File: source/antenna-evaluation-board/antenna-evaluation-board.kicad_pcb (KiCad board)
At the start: 4 copper layers, 129 x 69 mm, 41 parts, among them J1 Conn_Coaxial, J10 Conn_Coaxial, J2 Conn_Coaxial, J3 Conn_Coaxial, J4 Conn_Coaxial, J5 Conn_Coaxial, J6 Conn_Coaxial, J7 Conn_Coaxial, J8 Conn_Coaxial, J9 Conn_Coaxial

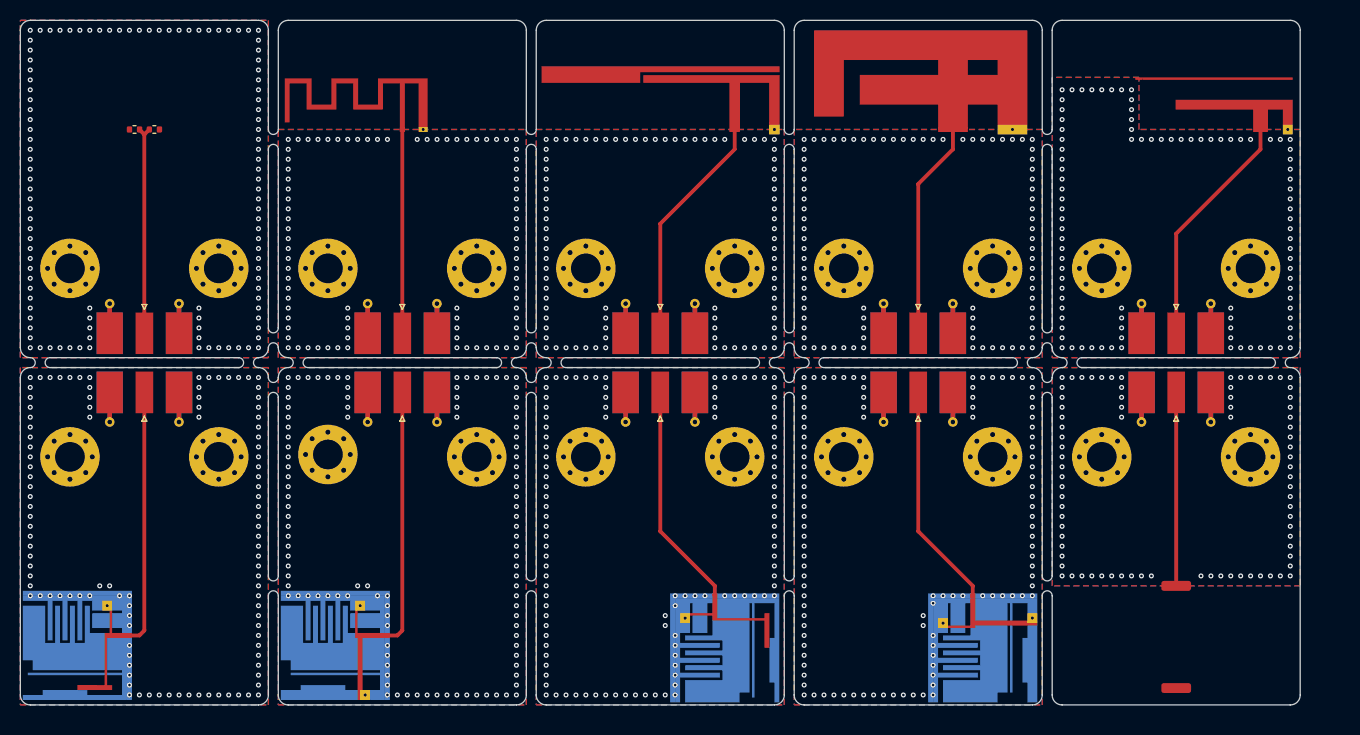
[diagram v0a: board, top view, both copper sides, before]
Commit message: use tons of drils instead of v cuts
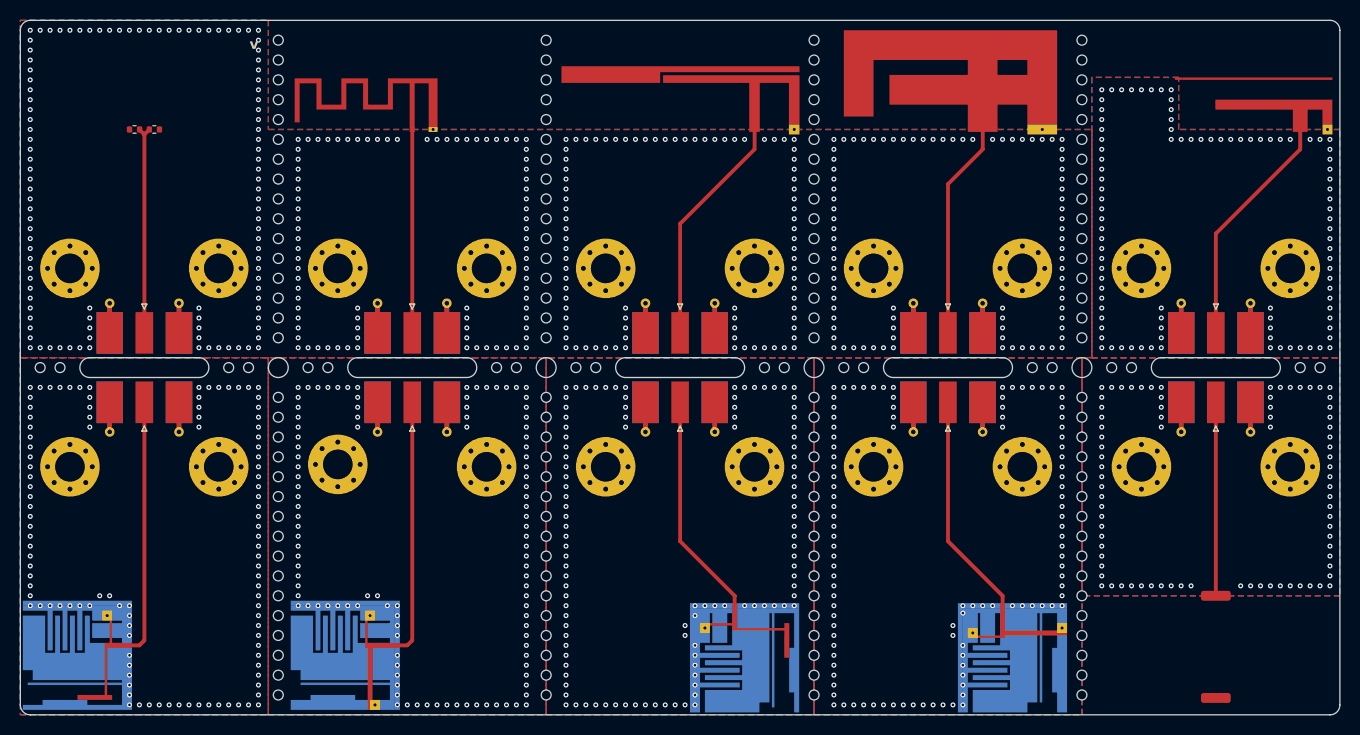
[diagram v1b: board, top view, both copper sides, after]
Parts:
- added REF**: MountingHole_2.1mm, MountingHole:MountingHole_2.1mm, F.Cu at (137.0, 81.0)
- added REF**: MountingHole_2.1mm, MountingHole:MountingHole_2.1mm, F.Cu at (137.0, 63.0)
- added REF**: MountingHole_2.1mm, MountingHole:MountingHole_2.1mm, F.Cu at (78.0, 74.0)
- added REF**: MountingHole_2.1mm, MountingHole:MountingHole_2.1mm, F.Cu at (110.0, 53.0)
- added REF**: MountingHole_2.1mm, MountingHole:MountingHole_2.1mm, F.Cu at (110.0, 93.0)
- added REF**: MountingHole_2.1mm, MountingHole:MountingHole_2.1mm, F.Cu at (137.0, 79.0)
- added REF**: MountingHole_2.1mm, MountingHole:MountingHole_2.1mm, F.Cu at (32.0, 74.0)
- added REF**: MountingHole_2.1mm, MountingHole:MountingHole_2.1mm, F.Cu at (56.0, 89.0)
- added REF**: MountingHole_2.1mm, MountingHole:MountingHole_2.1mm, F.Cu at (83.0, 87.0)
- added REF**: MountingHole_2.1mm, MountingHole:MountingHole_2.1mm, F.Cu at (110.0, 67.0)
- added REF**: MountingHole_2.1mm, MountingHole:MountingHole_2.1mm, F.Cu at (110.0, 47.0)
- added REF**: MountingHole_2.1mm, MountingHole:MountingHole_2.1mm, F.Cu at (137.0, 93.0)
- added REF**: MountingHole_2.1mm, MountingHole:MountingHole_2.1mm, F.Cu at (56.0, 65.0)
- added REF**: MountingHole_2.1mm, MountingHole:MountingHole_2.1mm, F.Cu at (83.0, 43.0)
- added REF**: MountingHole_2.1mm, MountingHole:MountingHole_2.1mm, F.Cu at (83.0, 97.0)
- added REF**: MountingHole_2.1mm, MountingHole:MountingHole_2.1mm, F.Cu at (83.0, 81.0)
- added REF**: MountingHole_2.1mm, MountingHole:MountingHole_2.1mm, F.Cu at (137.0, 43.0)
- added REF**: MountingHole_2.1mm, MountingHole:MountingHole_2.1mm, F.Cu at (83.0, 55.0)
- added REF**: MountingHole_2.1mm, MountingHole:MountingHole_2.1mm, F.Cu at (83.0, 41.0)
- added REF**: MountingHole_2.1mm, MountingHole:MountingHole_2.1mm, F.Cu at (110.0, 89.0)
- added REF**: MountingHole_2.1mm, MountingHole:MountingHole_2.1mm, F.Cu at (110.0, 61.0)
- added REF**: MountingHole_2.1mm, MountingHole:MountingHole_2.1mm, F.Cu at (56.0, 97.0)
- added REF**: MountingHole_2.1mm, MountingHole:MountingHole_2.1mm, F.Cu at (140.0, 74.0)
- added REF**: MountingHole_2.1mm, MountingHole:MountingHole_2.1mm, F.Cu at (137.0, 101.0)
- added REF**: MountingHole_2.1mm, MountingHole:MountingHole_2.1mm, F.Cu at (110.0, 83.0)
- added REF**: MountingHole_2.1mm, MountingHole:MountingHole_2.1mm, F.Cu at (115.0, 74.0)
- added REF**: MountingHole_2.1mm, MountingHole:MountingHole_2.1mm, F.Cu at (56.0, 101.0)
- added REF**: MountingHole_2.1mm, MountingHole:MountingHole_2.1mm, F.Cu at (110.0, 95.0)
- added REF**: MountingHole_2.1mm, MountingHole:MountingHole_2.1mm, F.Cu at (83.0, 53.0)
- added REF**: MountingHole_2.1mm, MountingHole:MountingHole_2.1mm, F.Cu at (110.0, 59.0)
- added REF**: MountingHole_2.1mm, MountingHole:MountingHole_2.1mm, F.Cu at (137.0, 71.0)
- added REF**: MountingHole_2.1mm, MountingHole:MountingHole_2.1mm, F.Cu at (83.0, 65.0)
- added REF**: MountingHole_2.1mm, MountingHole:MountingHole_2.1mm, F.Cu at (83.0, 47.0)
- added REF**: MountingHole_2.1mm, MountingHole:MountingHole_2.1mm, F.Cu at (113.0, 74.0)
- added REF**: MountingHole_2.1mm, MountingHole:MountingHole_2.1mm, F.Cu at (110.0, 97.0)
- added REF**: MountingHole_2.1mm, MountingHole:MountingHole_2.1mm, F.Cu at (110.0, 85.0)
- added REF**: MountingHole_2.1mm, MountingHole:MountingHole_2.1mm, F.Cu at (56.0, 81.0)
- added REF**: MountingHole_2.1mm, MountingHole:MountingHole_2.1mm, F.Cu at (83.0, 71.0)
- added REF**: MountingHole_2.1mm, MountingHole:MountingHole_2.1mm, F.Cu at (110.0, 57.0)
- added REF**: MountingHole_2.1mm, MountingHole:MountingHole_2.1mm, F.Cu at (83.0, 105.0)
- added REF**: MountingHole_2.1mm, MountingHole:MountingHole_2.1mm, F.Cu at (83.0, 67.0)
- added REF**: MountingHole_2.1mm, MountingHole:MountingHole_2.1mm, F.Cu at (56.0, 83.0)
- added REF**: MountingHole_2.1mm, MountingHole:MountingHole_2.1mm, F.Cu at (110.0, 63.0)
- added REF**: MountingHole_2.1mm, MountingHole:MountingHole_2.1mm, F.Cu at (56.0, 103.0)
- added REF**: MountingHole_2.1mm, MountingHole:MountingHole_2.1mm, F.Cu at (56.0, 95.0)
- added REF**: MountingHole_2.1mm, MountingHole:MountingHole_2.1mm, F.Cu at (34.0, 74.0)
- added REF**: MountingHole_2.1mm, MountingHole:MountingHole_2.1mm, F.Cu at (110.0, 99.0)
- added REF**: MountingHole_2.1mm, MountingHole:MountingHole_2.1mm, F.Cu at (137.0, 83.0)
- added REF**: MountingHole_2.1mm, MountingHole:MountingHole_2.1mm, F.Cu at (83.0, 61.0)
- added REF**: MountingHole_2.1mm, MountingHole:MountingHole_2.1mm, F.Cu at (137.0, 49.0)
- added REF**: MountingHole_2.1mm, MountingHole:MountingHole_2.1mm, F.Cu at (56.0, 87.0)
- added REF**: MountingHole_2.1mm, MountingHole:MountingHole_2.1mm, F.Cu at (134.0, 74.0)
- added REF**: MountingHole_2.1mm, MountingHole:MountingHole_2.1mm, F.Cu at (161.0, 74.0)
- added REF**: MountingHole_2.1mm, MountingHole:MountingHole_2.1mm, F.Cu at (137.0, 41.0)
- added REF**: MountingHole_2.1mm, MountingHole:MountingHole_2.1mm, F.Cu at (56.0, 93.0)
- added REF**: MountingHole_2.1mm, MountingHole:MountingHole_2.1mm, F.Cu at (83.0, 95.0)
- added REF**: MountingHole_2.1mm, MountingHole:MountingHole_2.1mm, F.Cu at (56.0, 63.0)
- added REF**: MountingHole_2.1mm, MountingHole:MountingHole_2.1mm, F.Cu at (56.0, 77.0)
- added REF**: MountingHole_2.1mm, MountingHole:MountingHole_2.1mm, F.Cu at (137.0, 45.0)
- added REF**: MountingHole_2.1mm, MountingHole:MountingHole_2.1mm, F.Cu at (56.0, 43.0)
- added REF**: MountingHole_2.1mm, MountingHole:MountingHole_2.1mm, F.Cu at (110.0, 101.0)
- added REF**: MountingHole_2.1mm, MountingHole:MountingHole_2.1mm, F.Cu at (110.0, 51.0)
- added REF**: MountingHole_2.1mm, MountingHole:MountingHole_2.1mm, F.Cu at (137.0, 95.0)
- added REF**: MountingHole_2.1mm, MountingHole:MountingHole_2.1mm, F.Cu at (83.0, 63.0)
- added REF**: MountingHole_2.1mm, MountingHole:MountingHole_2.1mm, F.Cu at (83.0, 51.0)
- added REF**: MountingHole_2.1mm, MountingHole:MountingHole_2.1mm, F.Cu at (137.0, 53.0)
- added REF**: MountingHole_2.1mm, MountingHole:MountingHole_2.1mm, F.Cu at (83.0, 49.0)
- added REF**: MountingHole_2.1mm, MountingHole:MountingHole_2.1mm, F.Cu at (110.0, 81.0)
- added REF**: MountingHole_2.1mm, MountingHole:MountingHole_2.1mm, F.Cu at (137.0, 105.0)
- added REF**: MountingHole_2.1mm, MountingHole:MountingHole_2.1mm, F.Cu at (83.0, 101.0)
- added REF**: MountingHole_2.1mm, MountingHole:MountingHole_2.1mm, F.Cu at (56.0, 85.0)
- added REF**: MountingHole_2.1mm, MountingHole:MountingHole_2.1mm, F.Cu at (137.0, 85.0)
- added REF**: MountingHole_2.1mm, MountingHole:MountingHole_2.1mm, F.Cu at (56.0, 49.0)
- added REF**: MountingHole_2.1mm, MountingHole:MountingHole_2.1mm, F.Cu at (56.0, 79.0)
- added REF**: MountingHole_2.1mm, MountingHole:MountingHole_2.1mm, F.Cu at (137.0, 97.0)
- added REF**: MountingHole_2.1mm, MountingHole:MountingHole_2.1mm, F.Cu at (110.0, 65.0)
- added REF**: MountingHole_2.1mm, MountingHole:MountingHole_2.1mm, F.Cu at (56.0, 91.0)
- added REF**: MountingHole_2.1mm, MountingHole:MountingHole_2.1mm, F.Cu at (83.0, 103.0)
- added REF**: MountingHole_2.1mm, MountingHole:MountingHole_2.1mm, F.Cu at (110.0, 79.0)
- added REF**: MountingHole_2.1mm, MountingHole:MountingHole_2.1mm, F.Cu at (61.0, 74.0)
- added REF**: MountingHole_2.1mm, MountingHole:MountingHole_2.1mm, F.Cu at (56.0, 41.0)
- added REF**: MountingHole_2.1mm, MountingHole:MountingHole_2.1mm, F.Cu at (83.0, 77.0)
- added REF**: MountingHole_2.1mm, MountingHole:MountingHole_2.1mm, F.Cu at (110.0, 71.0)
- added REF**: MountingHole_2.1mm, MountingHole:MountingHole_2.1mm, F.Cu at (137.0, 91.0)
- added REF**: MountingHole_2.1mm, MountingHole:MountingHole_2.1mm, F.Cu at (137.0, 103.0)
- added REF**: MountingHole_2.1mm, MountingHole:MountingHole_2.1mm, F.Cu at (110.0, 103.0)
- added REF**: MountingHole_2.1mm, MountingHole:MountingHole_2.1mm, F.Cu at (56.0, 71.0)
- added REF**: MountingHole_2.1mm, MountingHole:MountingHole_2.1mm, F.Cu at (56.0, 67.0)
- added REF**: MountingHole_2.1mm, MountingHole:MountingHole_2.1mm, F.Cu at (137.0, 107.0)
- added REF**: MountingHole_2.1mm, MountingHole:MountingHole_2.1mm, F.Cu at (110.0, 105.0)
- added REF**: MountingHole_2.1mm, MountingHole:MountingHole_2.1mm, F.Cu at (83.0, 45.0)
- added REF**: MountingHole_2.1mm, MountingHole:MountingHole_2.1mm, F.Cu at (132.0, 74.0)
- added REF**: MountingHole_2.1mm, MountingHole:MountingHole_2.1mm, F.Cu at (56.0, 99.0)
- added REF**: MountingHole_2.1mm, MountingHole:MountingHole_2.1mm, F.Cu at (83.0, 89.0)
- added REF**: MountingHole_2.1mm, MountingHole:MountingHole_2.1mm, F.Cu at (137.0, 87.0)
- added REF**: MountingHole_2.1mm, MountingHole:MountingHole_2.1mm, F.Cu at (56.0, 55.0)
- added REF**: MountingHole_2.1mm, MountingHole:MountingHole_2.1mm, F.Cu at (110.0, 107.0)
- added REF**: MountingHole_2.1mm, MountingHole:MountingHole_2.1mm, F.Cu at (83.0, 57.0)
- added REF**: MountingHole_2.1mm, MountingHole:MountingHole_2.1mm, F.Cu at (83.0, 91.0)
- added REF**: MountingHole_2.1mm, MountingHole:MountingHole_2.1mm, F.Cu at (137.0, 77.0)
- added REF**: MountingHole_2.1mm, MountingHole:MountingHole_2.1mm, F.Cu at (83.0, 99.0)
- added REF**: MountingHole_2.1mm, MountingHole:MountingHole_2.1mm, F.Cu at (110.0, 87.0)
- added REF**: MountingHole_2.1mm, MountingHole:MountingHole_2.1mm, F.Cu at (56.0, 47.0)
- added REF**: MountingHole_2.1mm, MountingHole:MountingHole_2.1mm, F.Cu at (56.0, 61.0)
- added REF**: MountingHole_2.1mm, MountingHole:MountingHole_2.1mm, F.Cu at (110.0, 49.0)
- added REF**: MountingHole_2.1mm, MountingHole:MountingHole_2.1mm, F.Cu at (59.0, 74.0)
- added REF**: MountingHole_2.1mm, MountingHole:MountingHole_2.1mm, F.Cu at (83.0, 69.0)
- added REF**: MountingHole_2.1mm, MountingHole:MountingHole_2.1mm, F.Cu at (137.0, 57.0)
- added REF**: MountingHole_2.1mm, MountingHole:MountingHole_2.1mm, F.Cu at (56.0, 69.0)
- added REF**: MountingHole_2.1mm, MountingHole:MountingHole_2.1mm, F.Cu at (137.0, 89.0)
- added REF**: MountingHole_2.1mm, MountingHole:MountingHole_2.1mm, F.Cu at (107.0, 74.0)
- added REF**: MountingHole_2.1mm, MountingHole:MountingHole_2.1mm, F.Cu at (137.0, 61.0)
- added REF**: MountingHole_2.1mm, MountingHole:MountingHole_2.1mm, F.Cu at (110.0, 77.0)
- added REF**: MountingHole_2.1mm, MountingHole:MountingHole_2.1mm, F.Cu at (110.0, 43.0)
- added REF**: MountingHole_2.1mm, MountingHole:MountingHole_2.1mm, F.Cu at (56.0, 51.0)
- added REF**: MountingHole_2.1mm, MountingHole:MountingHole_2.1mm, F.Cu at (56.0, 107.0)
- added REF**: MountingHole_2.1mm, MountingHole:MountingHole_2.1mm, F.Cu at (105.0, 74.0)
- added REF**: MountingHole_2.1mm, MountingHole:MountingHole_2.1mm, F.Cu at (110.0, 91.0)
- added REF**: MountingHole_2.1mm, MountingHole:MountingHole_2.1mm, F.Cu at (80.0, 74.0)
- added REF**: MountingHole_2.1mm, MountingHole:MountingHole_2.1mm, F.Cu at (83.0, 59.0)
- added REF**: MountingHole_2.1mm, MountingHole:MountingHole_2.1mm, F.Cu at (110.0, 69.0)
- added REF**: MountingHole_2.1mm, MountingHole:MountingHole_2.1mm, F.Cu at (86.0, 74.0)
- added REF**: MountingHole_2.1mm, MountingHole:MountingHole_2.1mm, F.Cu at (83.0, 85.0)
- added REF**: MountingHole_2.1mm, MountingHole:MountingHole_2.1mm, F.Cu at (56.0, 57.0)
- added REF**: MountingHole_2.1mm, MountingHole:MountingHole_2.1mm, F.Cu at (51.0, 74.0)
- added REF**: MountingHole_2.1mm, MountingHole:MountingHole_2.1mm, F.Cu at (83.0, 83.0)
- added REF**: MountingHole_2.1mm, MountingHole:MountingHole_2.1mm, F.Cu at (83.0, 93.0)
- added REF**: MountingHole_2.1mm, MountingHole:MountingHole_2.1mm, F.Cu at (137.0, 55.0)
- added REF**: MountingHole_2.1mm, MountingHole:MountingHole_2.1mm, F.Cu at (83.0, 107.0)
- added REF**: MountingHole_2.1mm, MountingHole:MountingHole_2.1mm, F.Cu at (137.0, 69.0)
- added REF**: MountingHole_2.1mm, MountingHole:MountingHole_2.1mm, F.Cu at (110.0, 41.0)
- added REF**: MountingHole_2.1mm, MountingHole:MountingHole_2.1mm, F.Cu at (110.0, 55.0)
- added REF**: MountingHole_2.1mm, MountingHole:MountingHole_2.1mm, F.Cu at (137.0, 65.0)
- added REF**: MountingHole_2.1mm, MountingHole:MountingHole_2.1mm, F.Cu at (137.0, 99.0)
- added REF**: MountingHole_2.1mm, MountingHole:MountingHole_2.1mm, F.Cu at (53.0, 74.0)
- added REF**: MountingHole_2.1mm, MountingHole:MountingHole_2.1mm, F.Cu at (88.0, 74.0)
- added REF**: MountingHole_2.1mm, MountingHole:MountingHole_2.1mm, F.Cu at (159.0, 74.0)
- added REF**: MountingHole_2.1mm, MountingHole:MountingHole_2.1mm, F.Cu at (56.0, 45.0)
- added REF**: MountingHole_2.1mm, MountingHole:MountingHole_2.1mm, F.Cu at (137.0, 47.0)
- added REF**: MountingHole_2.1mm, MountingHole:MountingHole_2.1mm, F.Cu at (56.0, 105.0)
- added REF**: MountingHole_2.1mm, MountingHole:MountingHole_2.1mm, F.Cu at (142.0, 74.0)
- added REF**: MountingHole_2.1mm, MountingHole:MountingHole_2.1mm, F.Cu at (56.0, 59.0)
- added REF**: MountingHole_2.1mm, MountingHole:MountingHole_2.1mm, F.Cu at (56.0, 53.0)
- added REF**: MountingHole_2.1mm, MountingHole:MountingHole_2.1mm, F.Cu at (137.0, 51.0)
- added REF**: MountingHole_2.1mm, MountingHole:MountingHole_2.1mm, F.Cu at (110.0, 45.0)
- added REF**: MountingHole_2.1mm, MountingHole:MountingHole_2.1mm, F.Cu at (137.0, 59.0)
- added REF**: MountingHole_2.1mm, MountingHole:MountingHole_2.1mm, F.Cu at (137.0, 67.0)
- added REF**: MountingHole_2.1mm, MountingHole:MountingHole_2.1mm, F.Cu at (83.0, 79.0)
- moved AE10 4.12 mm to (150.5, 97.0)
- moved H19 4.12 mm to (143.0, 84.0)
- moved H20 4.12 mm to (158.0, 84.0)
- moved J10 4.12 mm to (150.5, 77.5)
- moved J5 4.00 mm to (150.5, 70.5)
- moved AE4 4.00 mm to (159.0, 50.0)
- moved H10 4.00 mm to (158.0, 64.0)
- moved H9 4.00 mm to (143.0, 64.0)
- moved AE5 3.16 mm to (135.5, 108.8)
- moved H17 3.16 mm to (116.0, 84.0)
- moved H18 3.16 mm to (131.0, 84.0)
- moved J6 3.16 mm to (123.5, 77.5)
- moved J4 3.00 mm to (123.5, 70.5)
- moved AE3 3.00 mm to (127.0, 50.0)
- moved H7 3.00 mm to (116.0, 64.0)
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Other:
- board size 129 x 69 mm -> 133 x 70 mm
- board text added: "${title}"
- board text added: "v${revision}"
